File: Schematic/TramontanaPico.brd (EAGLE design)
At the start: 36 x 48 mm, 13 parts, among them U4 TEMT6000

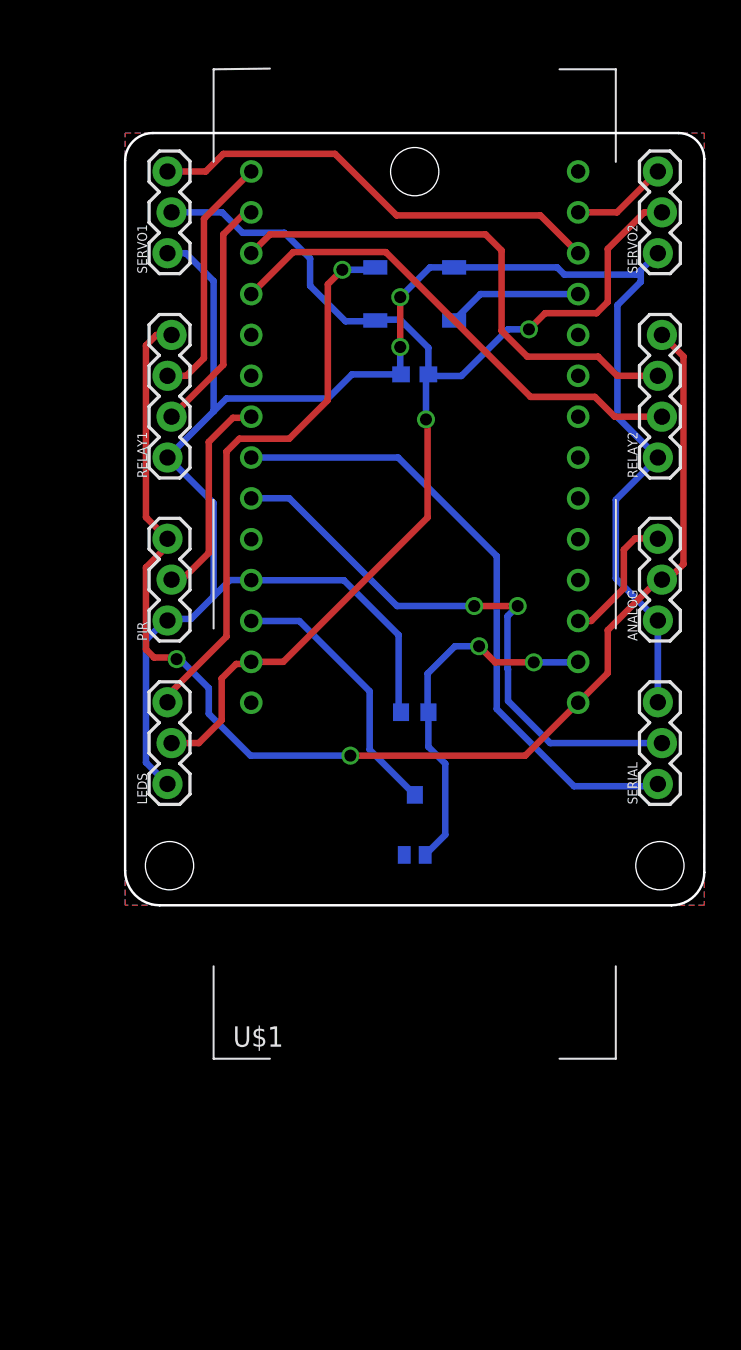
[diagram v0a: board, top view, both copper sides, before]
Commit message: added button
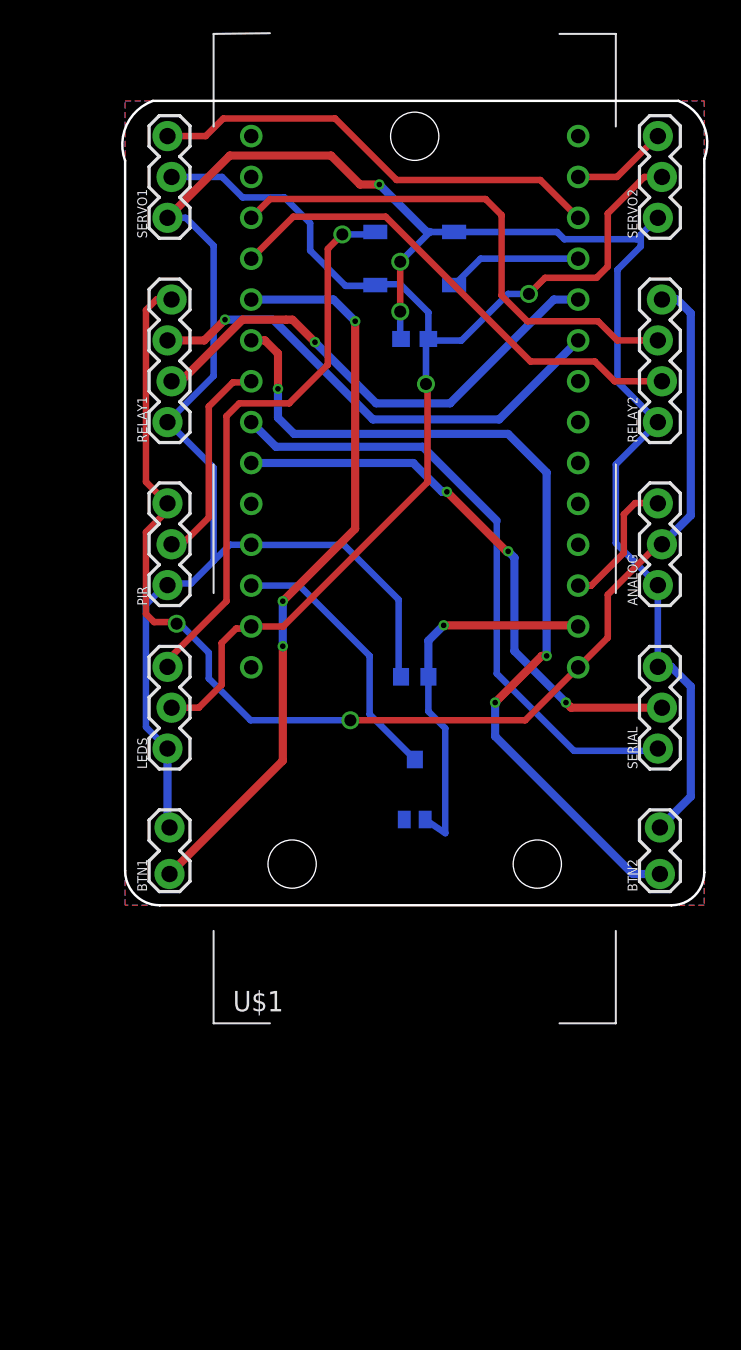
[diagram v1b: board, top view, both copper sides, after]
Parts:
- added BTN1, BTN2: (no value), SparkFun-Connectors:1X02_LOCK
- moved C4 2.20 mm to (18.0, 35.2)
- moved LED1 2.20 mm to (18.0, 40.2)
- moved SERVO1 2.20 mm to (2.76, 42.7)
- moved SERVO2 2.20 mm to (33.2, 42.7)
- moved LEDS 2.20 mm to (2.76, 9.74)
- moved SERIAL 2.20 mm to (33.2, 9.74)
- moved U4 2.20 mm to (18.0, 7.20)
- moved ANALOG 2.20 mm to (33.2, 19.9)
- moved PIR 2.20 mm to (2.76, 19.9)
- moved R2 2.20 mm to (18.0, 14.2)
- moved RELAY1 2.20 mm to (2.76, 30.0)
- moved RELAY2 2.20 mm to (33.2, 30.0)
- moved U$1 2.20 mm to (18.0, 23.4)
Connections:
- net N$10 renamed RST
- net N$19 renamed A2
- net N$20 renamed A3
- net N$21 renamed A4
- net N$22 renamed A5
- net N$23 renamed A6
- removed net N$24: U$1.0
- removed net N$25: U$1.1
- removed net N$5: U$1.10
- removed net N$6: U$1.11
- new net 0: RELAY1.3, U$1.0
- new net 1: RELAY1.2, U$1.1
- new net 10: BTN1.1, U$1.10
- new net 11: BTN2.1, U$1.11
- net 6: no longer RELAY1.3
- net 7: no longer RELAY1.2
- net GND: now also BTN1.2, BTN2.2
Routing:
- net 11: track 0.00 -> 55.8 mm, vias 0 -> 3
- net 10: track 0.00 -> 46.2 mm, vias 0 -> 3
- net 1: track 0.00 -> 31.7 mm, vias 0 -> 1
- net 0: track 0.00 -> 30.7 mm, vias 0 -> 1
- net GND: track 124.3 -> 148.7 mm, vias 2 -> 3
- net 6: track 15.5 -> 0.00 mm
- net 7: track 15.0 -> 0.00 mm
- net 5V: track 80.3 -> 81.4 mm
- net TX: track 36.2 -> 35.2 mm, vias 2 -> 3
- net A0: track 22.7 -> 23.6 mm, vias 2 -> 1
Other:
- board size 36 x 48 mm -> 36.4 x 50 mm

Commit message: improvements
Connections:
- net N$29 renamed 5
- removed net N$14: U$1.5V
- new net AREF: U$1.AREF
- net 5V: now also C4.1, LED1.1-VDD, LEDS.2, SERVO1.2, SERVO2.2, U$1.5V, U4.COLLECTOR; no longer U$1.AREF
- net VCC: no longer U4.COLLECTOR
- net VIN: no longer C4.1, LED1.1-VDD, LEDS.2, SERVO1.2, SERVO2.2
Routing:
- net VIN: track 75.2 -> 0.00 mm, vias 2 -> 0
- net 5V: track 81.4 -> 132.2 mm
- net VCC: track 16.8 -> 0.00 mm
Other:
- board text added: "/Users/pierluigi.dallarosa/Documents/eagle/Tramontana_Pico/_archive/SILK_BOTTOM_TramontanaPico.bmp"
- board text added: "/Users/pierluigi.dallarosa/Documents/eagle/Tramontana_Pico/_archive/SILK_TOP_TramontanaPico.bmp"

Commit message: pier's version
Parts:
- added HTTP: FRAME_DINA4_L, dp_devices:DP_LOGO
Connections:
- removed net 5V: ANALOG.2, C4.1, LED1.1-VDD, LEDS.2, PIR.3, RELAY1.4, RELAY2.4, SERVO1.2, SERVO2.2, U$1.5V, U4.COLLECTOR
- removed net VCC: U$1.VCC
- removed net VIN: U$1.VIN
- new net 5V_EXT: U$1.5V
- new net VCC_3V3: ANALOG.2, U$1.VCC
- new net VIN_5V: C4.1, LED1.1-VDD, LEDS.2, PIR.3, RELAY1.4, RELAY2.4, SERVO1.2, SERVO2.2, U$1.VIN, U4.COLLECTOR
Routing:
- net VIN_5V: track 0.00 -> 137.2 mm, vias 0 -> 3
- net 5V: track 132.2 -> 0.00 mm, vias 2 -> 0
- net VCC_3V3: track 0.00 -> 37.0 mm
- net TX: track 35.2 -> 37.9 mm
- net A0: track 23.6 -> 22.2 mm
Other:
- board size 36.4 x 50 mm -> 36.1 x 50 mm
